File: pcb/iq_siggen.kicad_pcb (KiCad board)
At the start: 4 copper layers, 100 x 100 mm, 303 parts, among them J1 J3 - BANK0, J10 Barrel_Jack_MountingPin, J11 Conn_Coaxial, J12 Conn_01x01_Male, J13 Conn_01x01_Male, J14 Conn_01x01_Male, J15 Conn_01x01_Male, J16 Conn_01x01_Male, J17 Conn_01x01_Male, J18 Conn_Coaxial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

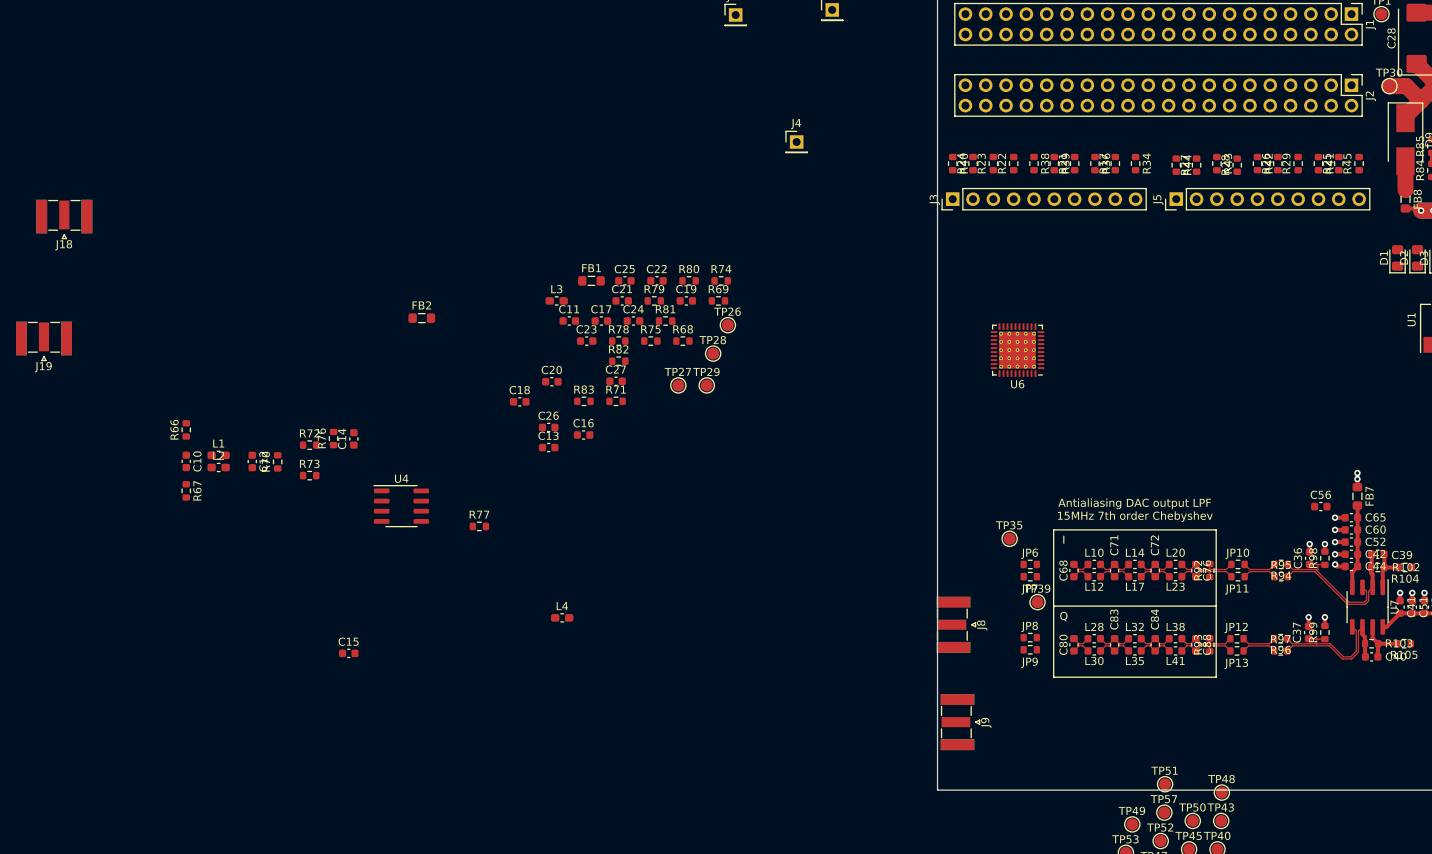
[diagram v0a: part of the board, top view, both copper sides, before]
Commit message: route A and B channels on input connector
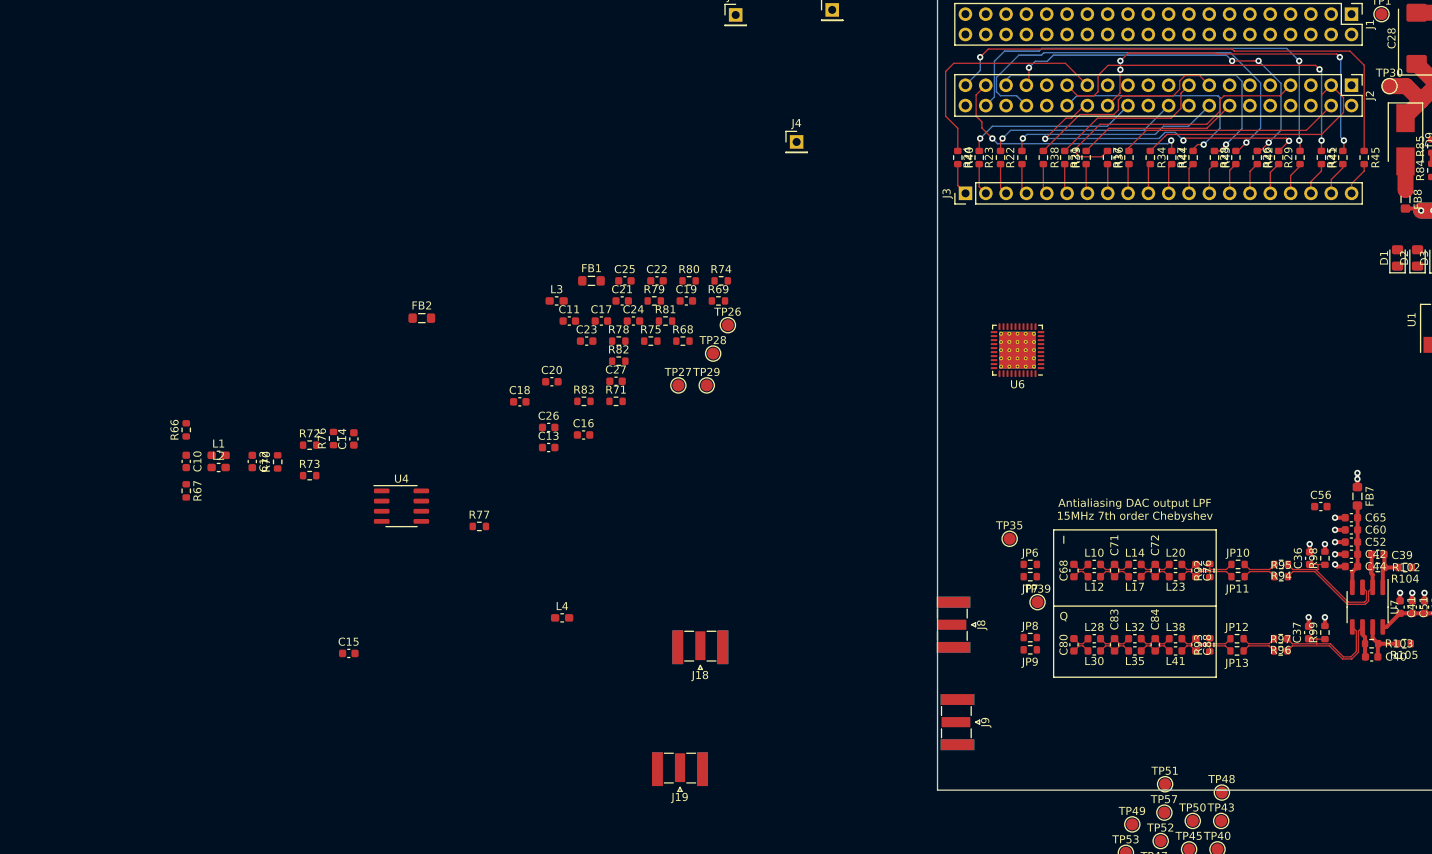
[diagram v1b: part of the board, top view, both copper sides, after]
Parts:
- removed J5: Conn_01x10_Male, Connector_PinHeader_2.54mm:PinHeader_1x10_P2.54mm_Vertical
- J3: value Conn_01x10_Male -> Conn_01x20_Male; footprint Connector_PinHeader_2.54mm:PinHeader_1x10_P2.54mm_Vertical -> Connector_PinHeader_2.54mm:PinHeader_1x20_P2.54mm_Vertical
- moved J18 96.0 mm to (20.4, 132.1)
- moved J19 96.0 mm to (17.8, 147.4)
- moved R34 1.99 mm to (76.6, 70.9)
- moved R17 1.87 mm to (73.9, 70.9)
- moved J3 1.76 mm to (53.5, 75.4)
- moved R36 1.75 mm to (71.3, 70.9)
- moved R21 1.63 mm to (68.6, 70.9)
- moved R39 1.51 mm to (65.9, 70.9)
- moved R38 1.40 mm to (63.2, 70.9)
- moved R22 1.29 mm to (60.6, 70.9)
- moved R23 1.18 mm to (57.9, 70.9)
- moved R44 1.11 mm to (79.3, 70.9)
- moved R24 1.08 mm to (55.2, 70.9)
- moved R27 1.05 mm to (81.9, 70.9)
- moved R40 0.99 mm to (52.5, 70.9)
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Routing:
- net Net-(J2-Pad39): track 0.00 -> 64.5 mm, vias 0 -> 1
- net Net-(J2-Pad38): track 0.00 -> 56.7 mm, vias 0 -> 2
- net Net-(J2-Pad34): track 0.00 -> 52.0 mm, vias 0 -> 1
- net Net-(J2-Pad26): track 0.00 -> 46.0 mm, vias 0 -> 4
- net Net-(J2-Pad33): track 0.00 -> 45.8 mm, vias 0 -> 4
- net Net-(J2-Pad29): track 0.00 -> 45.4 mm, vias 0 -> 2
- net Net-(J2-Pad35): track 0.00 -> 41.2 mm, vias 0 -> 1
- net Net-(J2-Pad28): track 0.00 -> 40.5 mm, vias 0 -> 3
- net Net-(J2-Pad7): track 0.00 -> 36.0 mm
- net Net-(J2-Pad3): track 0.00 -> 33.8 mm
- net Net-(J2-Pad37): track 0.00 -> 32.1 mm, vias 0 -> 2
- net Net-(J2-Pad27): track 0.00 -> 29.8 mm
- net Net-(J2-Pad30): track 0.00 -> 28.2 mm, vias 0 -> 1
- net Net-(J2-Pad4): track 0.00 -> 27.9 mm
- net Net-(J2-Pad16): track 0.00 -> 26.7 mm, vias 0 -> 1
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
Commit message: LO amp routing
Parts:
- removed C10, C11: 85p, Capacitor_SMD:C_0603_1608Metric
- removed C45, C46: 0.1u, Capacitor_SMD:C_0603_1608Metric
- removed JP10, JP11, JP12, JP13, JP6, JP7, JP8, JP9: Jumper, Resistor_SMD:R_0603_1608Metric
- removed L1, L2, L3, L4: 732n, Inductor_SMD:L_0603_1608Metric_Pad1.05x0.95mm_HandSolder
- removed R31: 100, Resistor_SMD:R_0603_1608Metric
- removed TP35, TP36, TP37, TP38, TP39, TP40, TP41, TP42, TP43, TP44, TP45, TP46, TP47, TP48, TP49, TP50: TestPoint, TestPoint:TestPoint_Pad_D1.5mm
- added JP4: SolderJumper_3_Open, iq_siggen:50ohm_solder_jumper, B.Cu at (107.0, 112.5)
- added JP5: SolderJumper_3_Open, iq_siggen:50ohm_solder_jumper, B.Cu at (107.0, 140.0)
- added R32: 0, Resistor_SMD:R_0603_1608Metric, F.Cu at (-33.4, 74.0)
- added R33: 0, Resistor_SMD:R_0603_1608Metric, F.Cu at (-33.4, 72.4)
- C12, C13: value 187p -> DNI
- R11, R12, R13, R14, R15, R16, R30, R5, R6, R7: value 100 -> 0
- R46, R47, R54, R55: value 22 -> DNI
- R66, R68: value 25 -> DNI
- R67, R69: value 25 -> 0
- R70, R71: value 50 -> 100
- R92, R93: value 50 -> DNI
- moved R16 286.4 mm to (-43.8, 78.4), turned to 180 degrees
- moved R5 212.9 mm to (62.9, 132.5)
- moved R4 208.6 mm to (62.9, 131.0)
- moved R30 182.1 mm to (87.6, 132.7)
- moved R12 178.0 mm to (87.6, 131.0)
- moved R2 174.3 mm to (62.2, 121.5)
- moved R11 170.2 mm to (87.6, 123.4)
- moved R3 170.1 mm to (62.4, 123.5)
- moved R10 168.2 mm to (87.6, 121.7)
- moved TP56 64.8 mm to (188.0, 146.5)
- moved TP53 63.6 mm to (61.6, 95.3), turned to 270 degrees
- moved TP52 58.6 mm to (63.1, 99.7), turned to 270 degrees
- moved R69 57.0 mm to (-33.4, 78.4)
- moved R68 56.4 mm to (-35.8, 77.6), turned to 90 degrees
- moved TP57 54.0 mm to (66.7, 100.1), turned to 270 degrees
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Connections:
- net Net-(C12-Pad1) renamed /mixer/CLK_I_1_P
- net Net-(C12-Pad2) renamed /mixer/CLK_I_1_N
- net Net-(C14-Pad1) renamed /mixer/CLK_I_2_P
- net Net-(C15-Pad1) renamed /mixer/CLK_Q_2_P
- net Net-(C22-Pad2) renamed /mixer/CLK_I_2_N
- net Net-(C23-Pad2) renamed /mixer/CLK_Q_2_N
- net Net-(J8-Pad1) renamed /CLK_EXT_IN_Connector
- net Net-(J9-Pad1) renamed /CLK_OUT_connector
- C13 pad 1: Net-(C13-Pad1) -> /mixer/CLK_Q_1_P
- C13 pad 2: Net-(C13-Pad2) -> /mixer/CLK_Q_1_N
- J1 pad 16: Net-(J1-Pad16) -> /Q_CLK_N
- J1 pad 18: Net-(J1-Pad18) -> /Q_CLK_P
- J1 pad 27: Net-(J1-Pad27) -> /I_CLK_N
- J1 pad 30: Net-(J1-Pad30) -> /I_CLK_P
- J18 pad 1: (no net) -> /mixer/LO_I_EXT
- J19 pad 1: (no net) -> /mixer/LO_Q_EXT
- R10 pad 1: Net-(J1-Pad27) -> /IQ DAC and AA filter/I AA Filter/50R_OUT_P
- R10 pad 2: /I_CLK_N -> /IQ DAC and AA filter/I_F_P
- R11 pad 1: /I_CLK_P -> /IQ DAC and AA filter/I AA Filter/50R_OUT_N
- R11 pad 2: /I_CLK_N -> /IQ DAC and AA filter/I_F_N
- R12 pad 1: /Q_CLK_P -> /IQ DAC and AA filter/Q AA filter/50R_OUT_P
- R12 pad 2: /Q_CLK_N -> /IQ DAC and AA filter/Q_F_P
- R2 pad 1: /Q_CLK_N -> /IQ DAC and AA filter/A_IOUT_P
- R2 pad 2: Net-(J1-Pad16) -> /IQ DAC and AA filter/I AA Filter/50R_IN_P
- R3 pad 1: /Q_CLK_P -> /IQ DAC and AA filter/A_IOUT_N
- R3 pad 2: Net-(J1-Pad18) -> /IQ DAC and AA filter/I AA Filter/50R_IN_N
- R30 pad 1: /mixer/CLK_I_N -> /IQ DAC and AA filter/Q AA filter/50R_OUT_N
- R30 pad 2: /mixer/CLK_I_P -> /IQ DAC and AA filter/Q_F_N
- R4 pad 1: /I_CLK_P -> /IQ DAC and AA filter/B_IOUT_P
- R4 pad 2: Net-(J1-Pad30) -> /IQ DAC and AA filter/Q AA filter/50R_IN_P
- R5 pad 1: /DAC_CLK_P -> /IQ DAC and AA filter/B_IOUT_N
- R5 pad 2: /DAC_CLK_N -> /IQ DAC and AA filter/Q AA filter/50R_IN_N
- R66 pad 1: /mixer/CLK_I_P -> /mixer/CLK_I_N
- R66 pad 2: GNDA -> /mixer/CLK_I_P
- R67 pad 1: /mixer/CLK_I_N -> /mixer/CLK_Q_P
- R67 pad 2: GNDA -> /mixer/CLK_Q_1_P
- R68 pad 1: /mixer/CLK_Q_P -> /mixer/CLK_Q_N
- R68 pad 2: GNDA -> /mixer/CLK_Q_P
- R69 pad 2: GNDA -> /mixer/CLK_Q_1_N
- R71 pad 1: Net-(C13-Pad2) -> /mixer/CLK_Q_1_N
- R71 pad 2: Net-(C13-Pad1) -> /mixer/CLK_Q_1_P
- R74 pad 2: Net-(C13-Pad1) -> /mixer/CLK_Q_1_P
- R75 pad 1: Net-(C13-Pad2) -> /mixer/CLK_Q_1_N
- T1 pad 1: (no net) -> /mixer/LO_Q
- T2 pad 1: (no net) -> /mixer/LO_I
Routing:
- net /mixer/LO_I_EXT: track 0.00 -> 61.5 mm, vias 0 -> 1
- net /mixer/LO_Q_EXT: track 0.00 -> 55.9 mm, vias 0 -> 1
- net /mixer/CLK_I_2_P: track 0.00 -> 16.9 mm
- net /mixer/CLK_I_2_N: track 0.00 -> 16.3 mm
- net /mixer/CLK_Q_2_P: track 0.00 -> 15.6 mm
- net /mixer/CLK_Q_2_N: track 0.00 -> 15.1 mm
- net /mixer/LO_I: track 0.00 -> 9.53 mm
- net /mixer/LO_Q: track 0.00 -> 8.78 mm
- net /mixer/-OPAMP_2.5V: track 0.00 -> 8.36 mm
- net /mixer/+OPAMP_2.5V: track 0.00 -> 8.00 mm
- net /mixer/CLK_Q_1_N: track 0.00 -> 6.41 mm
- net /mixer/CLK_I_1_N: track 0.00 -> 6.41 mm
- net /mixer/CLK_I_1_P: track 0.00 -> 6.41 mm
- net /mixer/CLK_Q_1_P: track 0.00 -> 6.41 mm
- net /mixer/CLK_Q_N: track 0.00 -> 2.14 mm
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
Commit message: clean up LO driver routing
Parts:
- removed TP14, TP15, TP16, TP26, TP27, TP28, TP29: TestPoint, TestPoint:TestPoint_Pad_D1.5mm
- added R31: 0, Resistor_SMD:R_0603_1608Metric, F.Cu at (141.7, 129.9)
- J11: footprint Connector_Coaxial:SMA_Samtec_SMA-J-P-X-ST-EM1_EdgeMount -> iq_siggen:SMA_Samtec_SMA-J-P-X-ST-EM1_EdgeMount_withSTEP
- moved R15 228.8 mm to (11.5, 86.5), turned to 270 degrees
- moved R100 160.9 mm to (62.8, 89.1)
- moved R16 54.3 mm to (9.90, 86.5), turned to 90 degrees
- moved R66 53.3 mm to (15.1, 88.9), turned to 180 degrees
- moved R33 52.8 mm to (15.9, 91.3), turned to 270 degrees
- moved R76 52.2 mm to (18.4, 101.7), turned to 180 degrees
- moved C14 52.0 mm to (18.4, 103.3), turned to 180 degrees
- moved R32 50.7 mm to (14.3, 91.3), turned to 270 degrees
- moved C12 50.5 mm to (15.1, 93.7), turned to 0 degrees
- moved R73 49.8 mm to (15.9, 97.7), turned to 270 degrees
- moved R70 49.7 mm to (15.1, 95.3), turned to 180 degrees
- moved C16 48.9 mm to (16.1, 111.4), turned to 90 degrees
- moved C19 48.7 mm to (16.0, 102.5), turned to 90 degrees
- moved R68 47.9 mm to (10.7, 88.9), turned to 0 degrees
- moved R72 47.6 mm to (14.3, 97.7), turned to 90 degrees
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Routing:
- net GNDA: track 66.1 -> 93.8 mm, vias 33 -> 53
- net Net-(C22-Pad1): track 0.00 -> 5.43 mm
- net Net-(C23-Pad1): track 0.00 -> 5.33 mm
- net /mixer/+OPAMP_2.5V: track 8.00 -> 13.2 mm, vias 0 -> 4
- net /mixer/-OPAMP_2.5V: track 8.36 -> 13.3 mm, vias 0 -> 4
- net /mixer/CLK_Q_2_N: track 15.1 -> 18.5 mm
- net /mixer/CLK_I_2_N: track 16.3 -> 19.5 mm
- net Net-(JP5-Pad1): track 0.00 -> 2.83 mm
- net Net-(JP4-Pad1): track 0.00 -> 1.69 mm
- net /mixer/RF_I: track 3.71 -> 2.21 mm
- net /mixer/RF_Q: track 3.68 -> 2.18 mm
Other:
- rule via_min_size: 0.45 -> 0.25

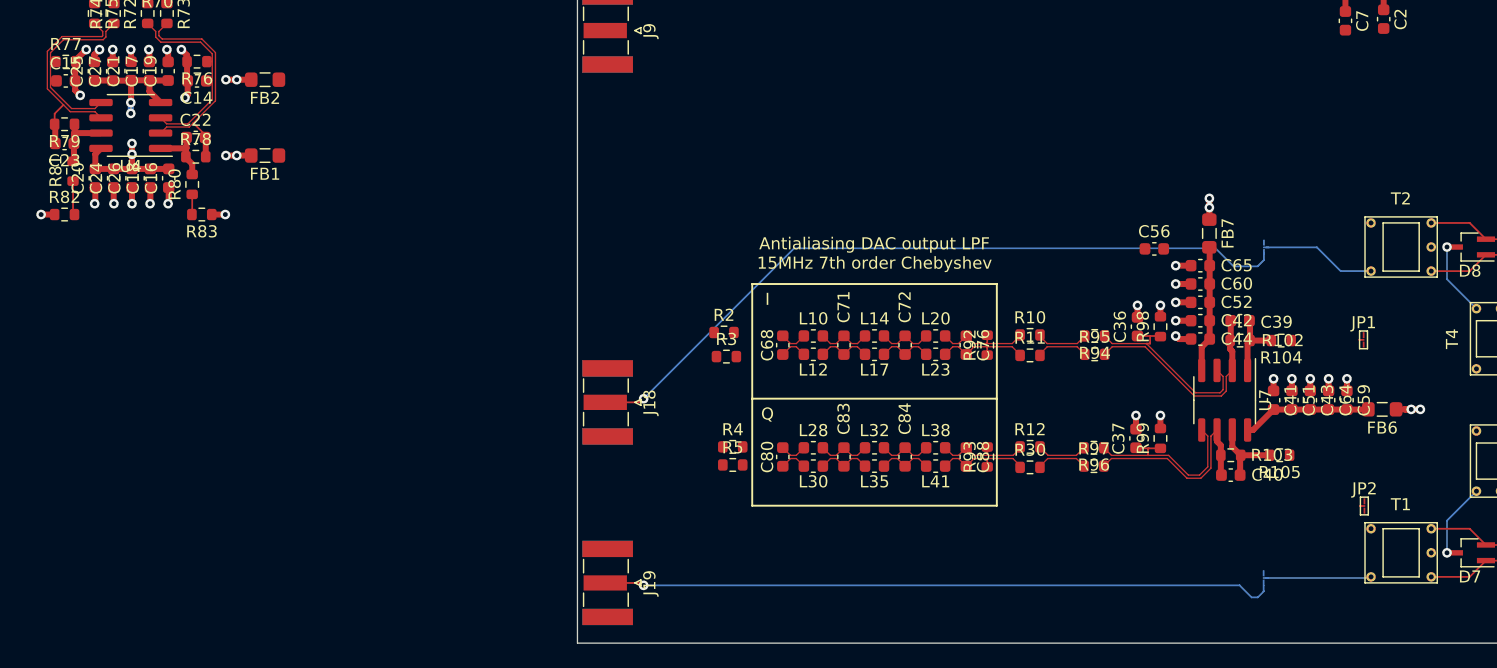
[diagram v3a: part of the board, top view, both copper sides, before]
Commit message: clean up baseband amplifier routing, make it like the LO amp
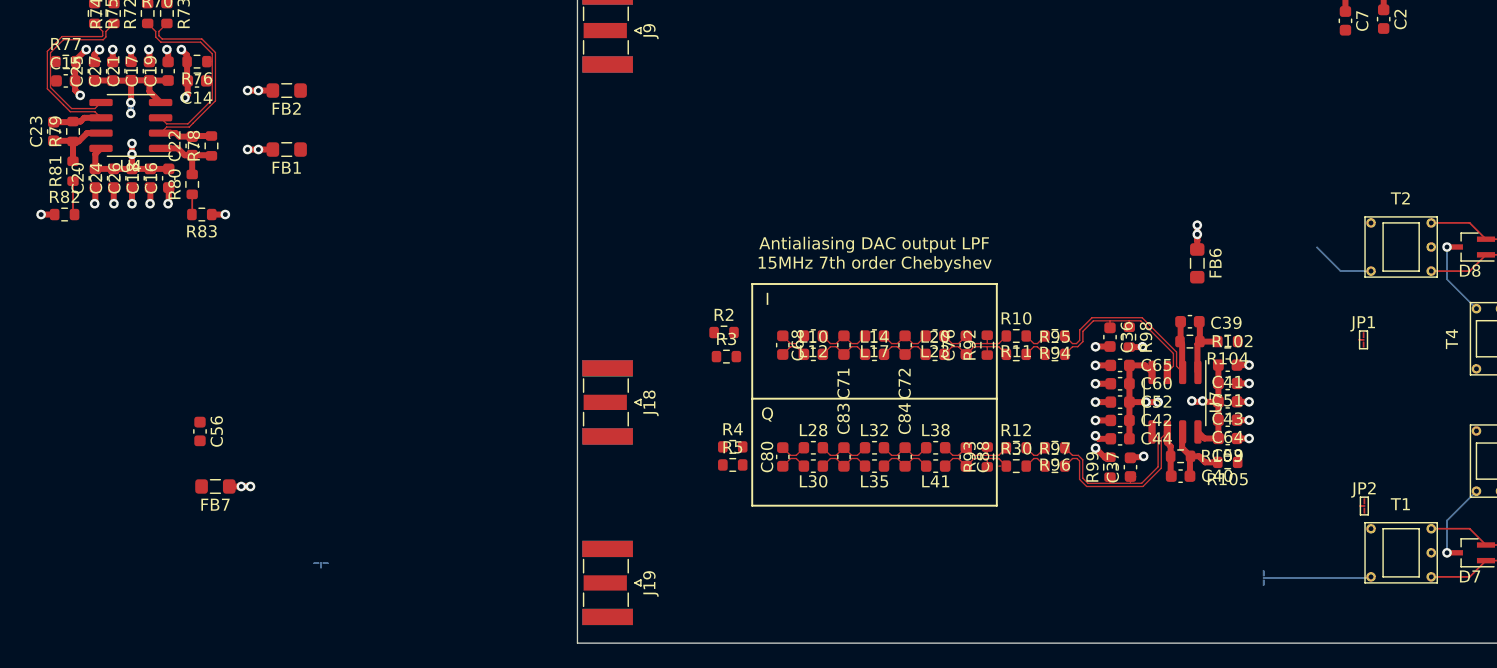
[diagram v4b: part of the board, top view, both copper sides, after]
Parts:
- R92, R93: value DNI -> 50
- moved FB7 85.2 mm to (19.9, 137.0), turned to 180 degrees
- moved JP4 81.4 mm to (30.6, 143.3), turned to 90 degrees
- moved C56 80.7 mm to (18.6, 132.4), turned to 270 degrees
- moved FB6 19.6 mm to (101.5, 118.5), turned to 270 degrees
- moved C52 10.6 mm to (95.1, 130.0)
- moved C60 10.6 mm to (95.1, 128.5)
- moved C65 10.6 mm to (95.1, 126.9)
- moved C42 10.6 mm to (95.1, 131.5)
- moved C44 10.6 mm to (95.1, 133.0)
- moved C59 10.4 mm to (104.0, 133.0), turned to 180 degrees
- moved C64 8.55 mm to (104.0, 131.5), turned to 180 degrees
- moved C43 6.86 mm to (104.0, 130.0), turned to 180 degrees
- moved C51 5.51 mm to (104.0, 128.4), turned to 180 degrees
- moved R99 4.82 mm to (94.2, 135.4)
- moved C41 4.80 mm to (104.0, 126.9), turned to 180 degrees
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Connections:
- R10 pad 1: /IQ DAC and AA filter/I AA Filter/50R_OUT_P -> /IQ DAC and AA filter/I AA Filter/50R_OUT_N
- R10 pad 2: /IQ DAC and AA filter/I_F_P -> /IQ DAC and AA filter/I_F_N
- R11 pad 1: /IQ DAC and AA filter/I AA Filter/50R_OUT_N -> /IQ DAC and AA filter/I AA Filter/50R_OUT_P
- R11 pad 2: /IQ DAC and AA filter/I_F_N -> /IQ DAC and AA filter/I_F_P
- R92 pad 1: /IQ DAC and AA filter/I AA Filter/50R_OUT_N -> /IQ DAC and AA filter/I AA Filter/50R_OUT_P
- R92 pad 2: /IQ DAC and AA filter/I AA Filter/50R_OUT_P -> /IQ DAC and AA filter/I AA Filter/50R_OUT_N
- R94 pad 1: /IQ DAC and AA filter/I_FB_P -> /IQ DAC and AA filter/I_FB_N
- R94 pad 2: /IQ DAC and AA filter/I_F_P -> /IQ DAC and AA filter/I_F_N
- R95 pad 1: /IQ DAC and AA filter/I_F_N -> /IQ DAC and AA filter/I_F_P
- R95 pad 2: /IQ DAC and AA filter/I_FB_N -> /IQ DAC and AA filter/I_FB_P
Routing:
- net /mixer/LO_I_EXT: track 61.5 -> 0.00 mm, vias 1 -> 0
- net /mixer/LO_Q_EXT: track 55.9 -> 0.00 mm, vias 1 -> 0
- net /mixer/LO_I: track 9.53 -> 5.30 mm
- net /IQ DAC and AA filter/Q_F_P: track 4.33 -> 2.08 mm
- net /IQ DAC and AA filter/I_F_P: track 4.27 -> 2.08 mm
- net /IQ DAC and AA filter/I_F_N: track 4.27 -> 2.08 mm
- net /IQ DAC and AA filter/Q_F_N: track 4.33 -> 2.25 mm
- net /IQ DAC and AA filter/I_FB_P: track 16.6 -> 14.7 mm
- net /mixer/CLK_I_2_N: track 19.5 -> 20.8 mm
- net /IQ DAC and AA filter/I AA Filter/50R_OUT_P: track 7.98 -> 6.89 mm
- net /IQ DAC and AA filter/I AA Filter/50R_OUT_N: track 7.97 -> 6.89 mm
- net /IQ DAC and AA filter/Q AA filter/50R_OUT_N: track 7.88 -> 6.83 mm
- net /IQ DAC and AA filter/Q AA filter/50R_OUT_P: track 7.88 -> 6.84 mm
- net GNDA: track 93.8 -> 94.7 mm
- net /IQ DAC and AA filter/Q_FB_P: track 15.6 -> 14.9 mm
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
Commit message: route power for amplifiers, fill zones for gnd and amplifiers
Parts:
- moved R53 192.2 mm to (58.3, 99.1), turned to 180 degrees
- moved R52 183.4 mm to (58.3, 84.1), turned to 180 degrees
- moved R55 178.2 mm to (55.9, 99.9), turned to 270 degrees
- moved R47 178.1 mm to (60.7, 99.9), turned to 270 degrees
- moved R46 175.6 mm to (60.7, 85.0), turned to 270 degrees
- moved R54 168.4 mm to (55.9, 85.0), turned to 270 degrees
- moved R59 135.7 mm to (118.3, 80.7), turned to 270 degrees
- moved R57 120.2 mm to (113.5, 80.7), turned to 270 degrees
- moved R58 113.9 mm to (115.9, 80.7), turned to 270 degrees
- moved R56 102.6 mm to (110.9, 80.7), turned to 270 degrees
- moved R82 99.6 mm to (106.2, 126.8), turned to 90 degrees
- moved R81 95.8 mm to (102.7, 126.1), turned to 180 degrees
- moved C23 95.0 mm to (99.3, 127.7), turned to 180 degrees
- moved C20 94.2 mm to (103.2, 124.2), turned to 180 degrees
- moved R79 93.1 mm to (99.3, 126.1), turned to 180 degrees
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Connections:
- JP1 pad 1: /mixer/IF_I -> /I_OUT
- JP1 pad 3: /I_OUT -> /mixer/IF_I
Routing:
- net -2V5: track 4.49 -> 81.6 mm, vias 2 -> 4
- net /mixer/LO_I_EXT: track 0.00 -> 67.8 mm, vias 0 -> 3
- net /mixer/LO_Q_EXT: track 0.00 -> 63.3 mm, vias 0 -> 1
- net +2V5: track 9.14 -> 70.2 mm, vias 2 -> 0
- net GNDA: track 94.7 -> 127.5 mm, vias 53 -> 73
- net /I_OUT: track 0.00 -> 30.1 mm
- net /Q_OUT: track 0.00 -> 30.0 mm
- net +5V: track 65.0 -> 88.0 mm, vias 2 -> 6
- net /IQ DAC and AA filter/I_DAC_OUT: track 0.00 -> 23.0 mm
- net Net-(JP5-Pad1): track 2.83 -> 25.1 mm, vias 0 -> 1
- net /IQ DAC and AA filter/Q_DAC_OUT: track 0.00 -> 20.8 mm
- net Net-(JP4-Pad1): track 1.69 -> 8.51 mm, vias 0 -> 1
- net /mixer/IF_I: track 0.00 -> 6.59 mm
- net /mixer/IF_Q: track 0.00 -> 6.58 mm
- net /IQ DAC and AA filter/-OPAMP_2.5V: track 10.2 -> 16.5 mm, vias 2 -> 6
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- added copper zone on In2.Cu, net /IQ DAC and AA filter/+OPAMP_2.5V
- added copper zone on In2.Cu, net /IQ DAC and AA filter/-OPAMP_2.5V
- added copper zone on In2.Cu, net /mixer/+OPAMP_2.5V
- added copper zone on In2.Cu, net /mixer/-OPAMP_2.5V
- added copper zone on In1.Cu, net GNDA
- added copper zone on In2.Cu, net GNDA
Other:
- rule via_min_drill: 0.23 -> 0.2
